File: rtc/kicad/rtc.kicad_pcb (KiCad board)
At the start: 2 copper layers, 62.5 x 34 mm, 11 parts, among them J1 Conn_RIOT, Q1 2N3904, U1 DS1305N, Y1 32.768khz

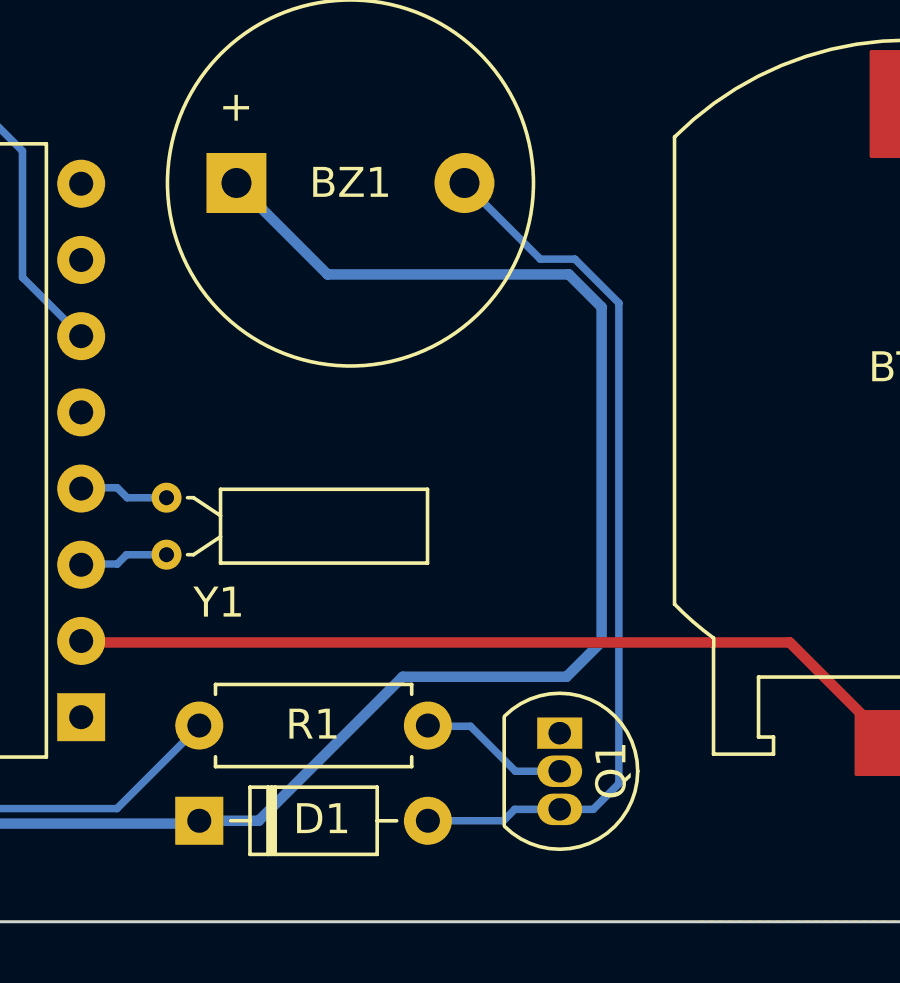
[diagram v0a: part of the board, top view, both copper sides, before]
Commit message: Change transistor pads to make soldering easier
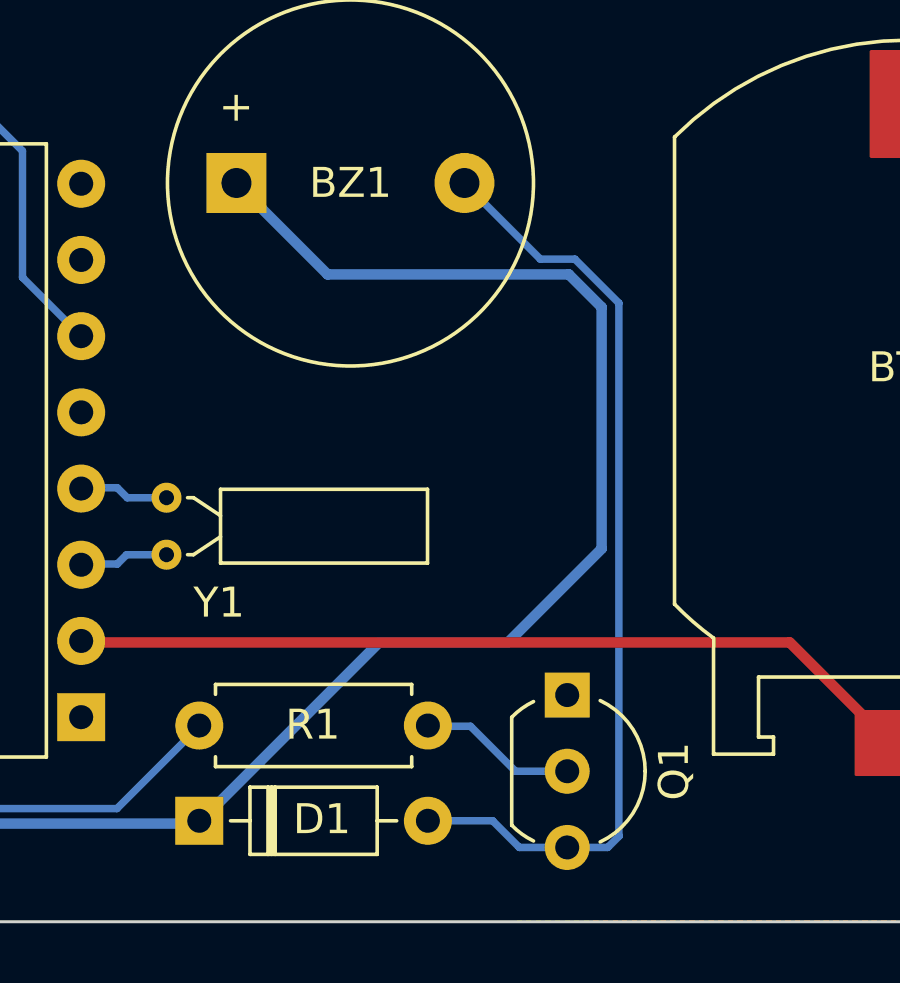
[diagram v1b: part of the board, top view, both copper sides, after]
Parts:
- Q1: footprint Package_TO_SOT_THT:TO-92_Inline -> Package_TO_SOT_THT:TO-92_Inline_Wide
- moved Q1 1.29 mm to (169.1, 96.4)
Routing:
- net VCC: track 96.1 -> 94.3 mm
- net Net-(BZ1-+): track 29.7 -> 31.4 mm
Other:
- board text added: "Ver. ${VERSION}"
- board text removed: "v1.0A"
